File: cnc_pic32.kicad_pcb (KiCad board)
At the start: 4 copper layers, 96 x 96 mm, 133 parts, among them J1 icd, J10 tp_ft232_, J11 tp_ft232_, J12 tp_ft232_, J13 tp_ft232_, J14 tp_ft232_, J15 pololu, J16 pololu, J17 pololu, J18 pololu, J19 pololu, J2 USB_B_Mini, J20 pololu, J21 conector oled ST1306 128x32, J22 Adafruit ST7789, J23 mrf24j40_tp, J24 mrf24j40_tp, J3 tp_ft232_, J4 tp_ft232_, J5 USB_B_Mini, J6 tp_ft232_, J7 tp_ft232_, J8 tp_ft232_, J9 tp_ft232_, Q1 2N7002, SW1 power, SW2 up, SW3 down, SW4 left, SW5 rigth, U1 PIC32MX795F512L-80x-PF, U2 LM1117DT-3.3, U3 FT232BM, U4 LM1117DT-3.3, U5 MRF24J40MA, Y1 8MHZ, Y2 6MHZ

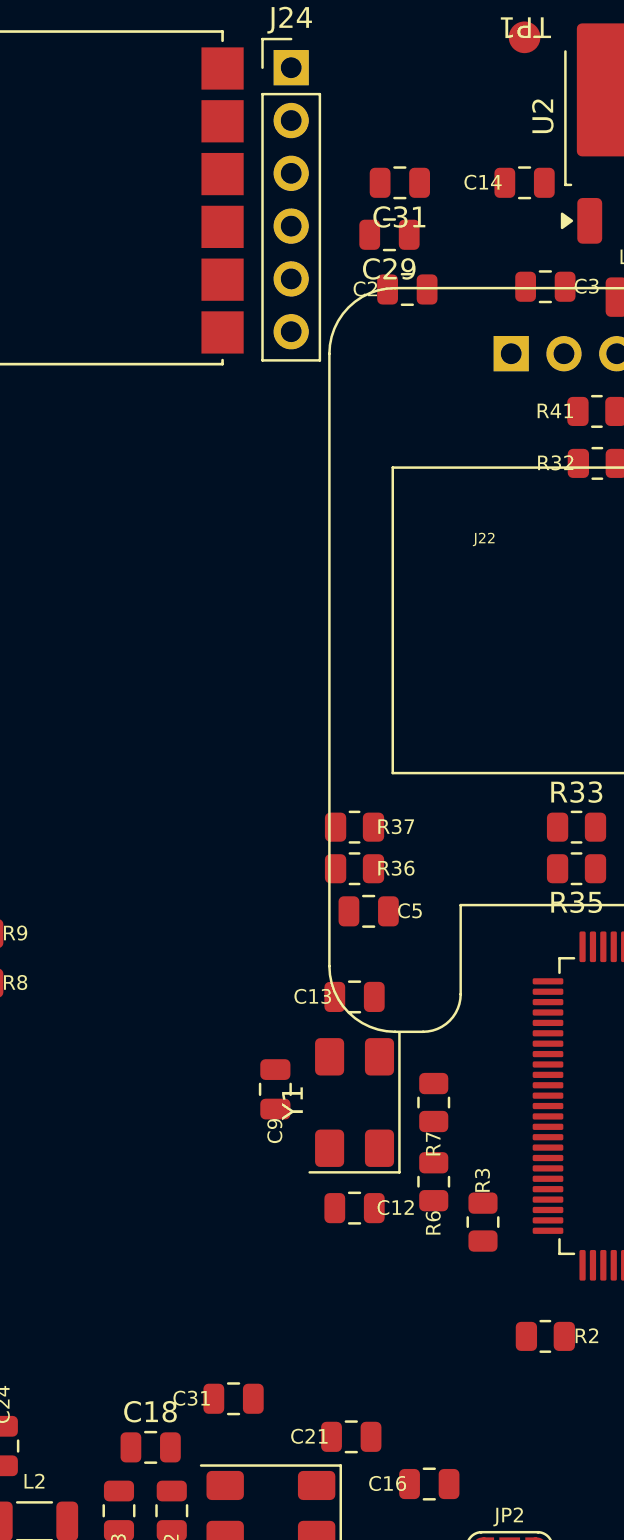
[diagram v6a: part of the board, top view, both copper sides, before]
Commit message: fix: remove duplicate C31 from PCB
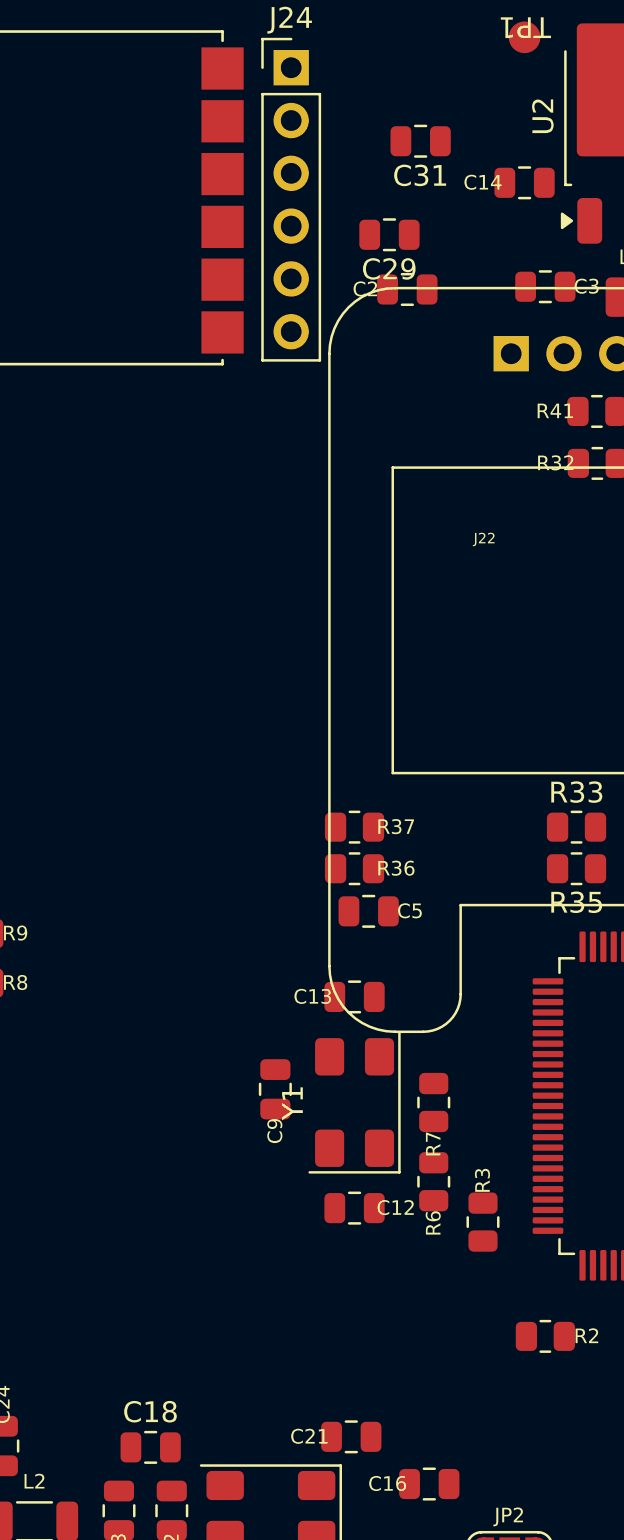
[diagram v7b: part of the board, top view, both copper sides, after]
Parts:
- removed the C31 at (78.0, 93.5)
- moved C31 2.24 mm to (87.0, 33.0)
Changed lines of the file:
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@@
 		)
 	)
-	(footprint "Capacitor_SMD:C_0805_2012Metric"
-		(layer "F.Cu")
-		(at 78 93.5)
-		(descr "Capacitor SMD 0805 (2012 Metric), square (rectangular) end terminal, IPC-7351 nominal, (Body size source: IPC-SM-782 page 76, https://www.pcb-3d.com/wordpress/wp-content/uploads/ipc-sm-782a_amendment_1_and_2.pdf, https://docs.google.com/spreadsheets/d/1BsfQQcO9C6DZCsRaXUlFlo91Tg2WpOkGARC1WS5S8t0/edit?usp=sharing)")
-		(tags "capacitor")
-		(property "Reference" "C31"
-			(at -2 0 0)
-			(layer "F.SilkS")
-			(effects
-				(font
-					(face "Arial")
-					(size 0.7 0.7)
-					(thickness 0.1)
-				)
-			)
-			(render_cache "C31" 0
-				(polygon
-					(pts
-						(xy 75.480764 93.181205) (xy 75.425794 93.186116) (xy 75.379489 93.200024) (xy 75.340185 93.222346)
-						(xy 75.306717 93.253397) (xy 75.280597 93.290873) (xy 75.261246 93.335369) (xy 75.248949 93.388238)
-						(xy 75.244569 93.451167) (xy 75.249039 93.513038) (xy 75.261707 93.566016) (xy 75.281863 93.611569)
-						(xy 75.309367 93.65086) (xy 75.344292 93.683659) (xy 75.384378 93.706983) (xy 75.430649 93.721356)
-						(xy 75.484611 93.726386) (xy 75.530032 93.722431) (xy 75.570486 93.710977) (xy 75.606918 93.692203)
-						(xy 75.640017 93.665715) (xy 75.67016 93.630569) (xy 75.697383 93.585336) (xy 75.772011 93.622778)
-						(xy 75.748537 93.66475) (xy 75.721301 93.70053) (xy 75.690244 93.730749) (xy 75.655111 93.755835)
-						(xy 75.616682 93.775477) (xy 75.575088 93.789691) (xy 75.529833 93.798433) (xy 75.480337 93.801442)
-						(xy 75.41354 93.796428) (xy 75.355269 93.782094) (xy 75.304109 93.759041) (xy 75.269143 93.735556)
-						(xy 75.238809 93.707741) (xy 75.212749 93.67532) (xy 75.190799 93.637823) (xy 75.169704 93.583928)
-						(xy 75.156468 93.522178) (xy 75.151818 93.451167) (xy 75.155749 93.385686) (xy 75.166919 93.328773)
-						(xy 75.184645 93.279202) (xy 75.208603 93.235938) (xy 75.238841 93.198174) (xy 75.275222 93.166025)
-						(xy 75.316658 93.140807) (xy 75.363876 93.122294) (xy 75.417865 93.110691) (xy 75.479824 93.10662)
-						(xy 75.534017 93.109517) (xy 75.581471 93.11776) (xy 75.623074 93.13083) (xy 75.659599 93.148422)
-						(xy 75.693157 93.171689) (xy 75.721836 93.199786) (xy 75.746005 93.233115) (xy 75.765771 93.272332)
-						(xy 75.679217 93.300841) (xy 75.66021 93.264768) (xy 75.635261 93.235404) (xy 75.603905 93.211937)
-						(xy 75.56814 93.19521) (xy 75.527431 93.184832)
-					)
-				)
-				(polygon
-					(pts
-						(xy 76.310823 93.60504) (xy 76.306765 93.651148) (xy 76.295302 93.689809) (xy 76.276963 93.722446)
-						(xy 76.25154 93.750065) (xy 76.220796 93.771418) (xy 76.183303 93.787432) (xy 76.137683 93.797734)
-						(xy 76.082236 93.801442) (xy 76.030765 93.798184) (xy 75.987179 93.789026) (xy 75.950239 93.774637)
-						(xy 75.918917 93.755322) (xy 75.892119 93.73016) (xy 75.871175 93.699656) (xy 75.855865 93.662941)
-						(xy 75.846512 93.61876) (xy 75.935459 93.610639) (xy 75.944756 93.648359) (xy 75.959694 93.677449)
-						(xy 75.979969 93.699647) (xy 76.006147 93.715929) (xy 76.039577 93.726383) (xy 76.082236 93.73019)
-						(xy 76.124477 93.726215) (xy 76.15788 93.715233) (xy 76.184348 93.697962) (xy 76.204299 93.674085)
-						(xy 76.216846 93.64293) (xy 76.221406 93.602219) (xy 76.216536 93.567486) (xy 76.202582 93.53924)
-						(xy 76.179091 93.515879) (xy 76.149237 93.499619) (xy 76.109438 93.488853) (xy 76.05689 93.484848)
-						(xy 76.008121 93.484848) (xy 76.008121 93.410262) (xy 76.054967 93.410262) (xy 76.101253 93.406371)
-						(xy 76.137089 93.39577) (xy 76.164729 93.379445) (xy 76.186239 93.356463) (xy 76.19917 93.328534)
-						(xy 76.203711 93.294088) (xy 76.199894 93.25936) (xy 76.189188 93.231413) (xy 76.17191 93.208731)
-						(xy 76.148778 93.192084) (xy 76.118064 93.181353) (xy 76.077449 93.177401) (xy 76.040549 93.180923)
-						(xy 76.010318 93.190806) (xy 75.985382 93.206594) (xy 75.965587 93.228158) (xy 75.951945 93.255109)
-						(xy 75.94452 93.288788) (xy 75.857967 93.282077) (xy 75.866174 93.2419) (xy 75.880366 93.20759)
-						(xy 75.900383 93.178172) (xy 75.926568 93.152995) (xy 75.957086 93.133289) (xy 75.992011 93.118849)
-						(xy 76.032125 93.109799) (xy 76.07839 93.10662) (xy 76.129448 93.109997) (xy 76.171789 93.119415)
-						(xy 76.206886 93.1341) (xy 76.235938 93.153722) (xy 76.260215 93.179171) (xy 76.277578 93.208898)
-						(xy 76.288351 93.243754) (xy 76.292145 93.284984) (xy 76.287846 93.326641) (xy 76.27569 93.36111)
-						(xy 76.256027 93.389917) (xy 76.229611 93.413082) (xy 76.195228 93.431449) (xy 76.151095 93.44467)
-						(xy 76.151095 93.446593) (xy 76.19968 93.456478) (xy 76.238239 93.473605) (xy 76.268722 93.4975)
-						(xy 76.29197 93.528193) (xy 76.305967 93.563571)
-					)
-				)
-				(polygon
-					(pts
-						(xy 76.428152 93.7905) (xy 76.428152 93.717324) (xy 76.599848 93.717324) (xy 76.599848 93.199798)
-						(xy 76.44777 93.309048) (xy 76.44777 93.227752) (xy 76.607029 93.117562) (xy 76.686402 93.117562)
-						(xy 76.686402 93.717324) (xy 76.850405 93.717324) (xy 76.850405 93.7905)
-					)
-				)
-			)
-		)
-		(property "Value" "33nf"
-			(at 0 0.8 0)
-			(layer "F.Fab")
-			(effects
-				(font
-					(size 0.5 0.5)
-					(thickness 0.15)
-				)
-			)
-		)
-		(property "Datasheet" ""
-			(at 0 0 0)
-			(layer "F.Fab")
-			(hide yes)
-			(effects
-				(font
-					(size 0.5 0.5)
-				)
-			)
-		)
-		(property "Description" ""
-			(at 0 0 0)
-			(layer "F.Fab")
-			(hide yes)
-			(effects
-				(font
-					(size 0.5 0.5)
-				)
-			)
-		)
-		(property ki_fp_filters "C_*")
-		(sheetname "/Ft232/")
-		(sheetfile "ft232.kicad_sch")
-		(units
-			(unit
-				(name "A")
-				(pins "1" "2")
-			)
-		)
-		(attr smd)
-		(duplicate_pad_numbers_are_jumpers no)
-		(fp_line
-			(start -0.261252 -0.735)
-			(end 0.261252 -0.735)
-			(stroke
-				(width 0.12)
-				(type solid)
-			)
-			(layer "F.SilkS")
-		)
-		(fp_line
-			(start -0.261252 0.735)
-			(end 0.261252 0.735)
-			(stroke
-				(width 0.12)
-				(type solid)
-			)
-			(layer "F.SilkS")
-		)
-		(fp_rect
-			(start -1.7 -0.98)
-			(end 1.7 0.98)
-			(stroke
-				(width 0.05)
-				(type solid)
-			)
-			(fill no)
-			(layer "F.CrtYd")
-		)
-		(fp_rect
-			(start -1 -0.625)
-			(end 1 0.625)
-			(stroke
-				(width 0.1)
-				(type solid)
-			)
-			(fill no)
-			(layer "F.Fab")
-		)
-		(fp_text user "${REFERENCE}"
-			(at 0 -0.8 0)
-			(layer "F.Fab")
-			(effects
-				(font
-					(size 0.5 0.5)
-					(thickness 0.08)
-				)
-			)
-		)
-		(pad "1" smd roundrect
-			(at -0.95 0)
-			(size 1 1.45)
-			(layers "F.Cu" "F.Mask" "F.Paste")
-			(roundrect_rratio 0.25)
-			(net "Net-(J3-Pin_1)")
-			(pintype "passive")
-		)
-		(pad "2" smd roundrect
-			(at 0.95 0)
-			(size 1 1.45)
-			(layers "F.Cu" "F.Mask" "F.Paste")
-			(roundrect_rratio 0.25)
-			(net "GND")
-			(pintype "passive")
-		)
-		(embedded_fonts no)
-		(model "${KICAD10_3DMODEL_DIR}/Capacitor_SMD.3dshapes/C_0805_2012Metric.step"
-			(offset
-				(xyz 0 0 0)
-			)
-			(scale
-				(xyz 1 1 1)
-			)
-			(rotate
-				(xyz 0 0 0)
-			)
-		)
-	)
 	(footprint "Jumper:SolderJumper-3_P1.3mm_Open_RoundedPad1.0x1.5mm_NumberLabels"
 		(layer "F.Cu")
@@
 	(footprint "Capacitor_SMD:C_0805_2012Metric"
 		(layer "F.Cu")
-		(at 86 35 180)
+		(at 87 33 180)
 		(descr "Capacitor SMD 0805 (2012 Metric), square (rectangular) end terminal, IPC-7351 nominal, (Body size source: IPC-SM-782 page 76, https://www.pcb-3d.com/wordpress/wp-content/uploads/ipc-sm-782a_amendment_1_and_2.pdf, https://docs.google.com/spreadsheets/d/1BsfQQcO9C6DZCsRaXUlFlo91Tg2WpOkGARC1WS5S8t0/edit?usp=sharing)")
 		(tags "capacitor")

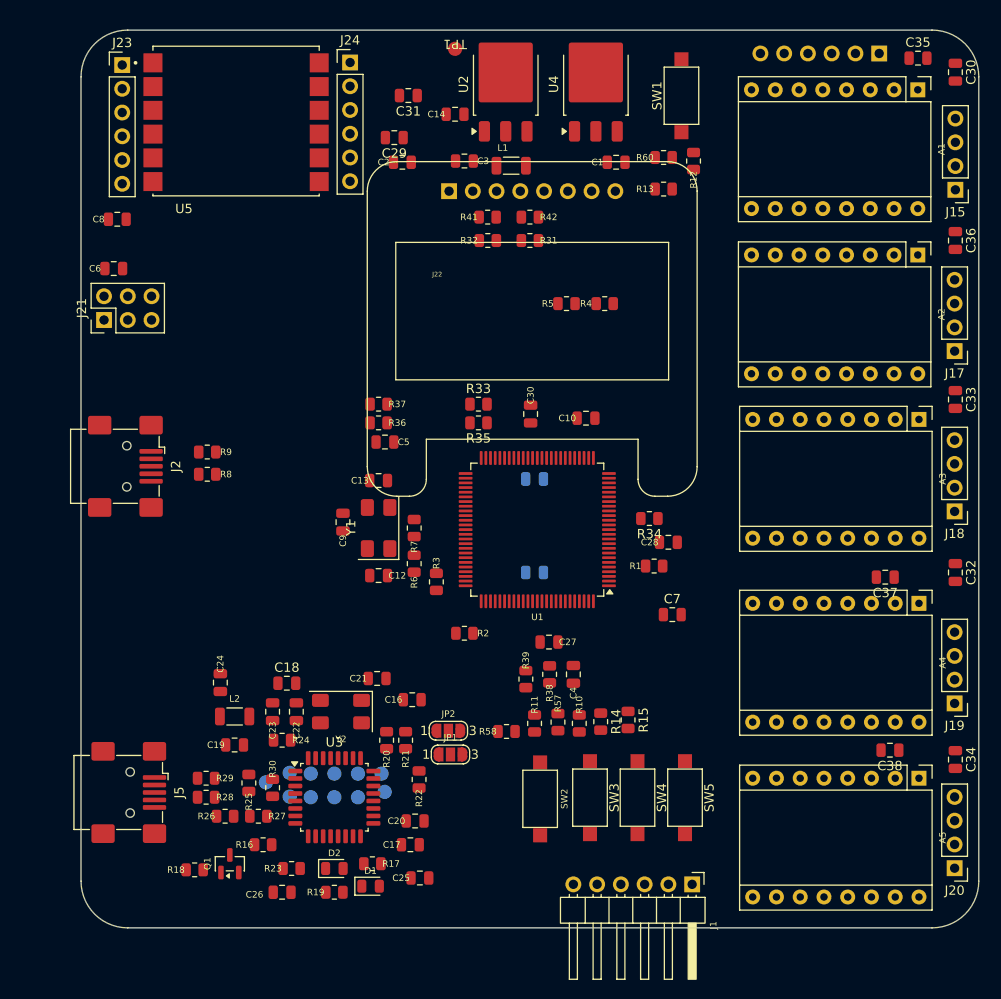
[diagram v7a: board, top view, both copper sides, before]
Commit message: feat: PCB layout updates, schematic changes, remove freerouting.dsn
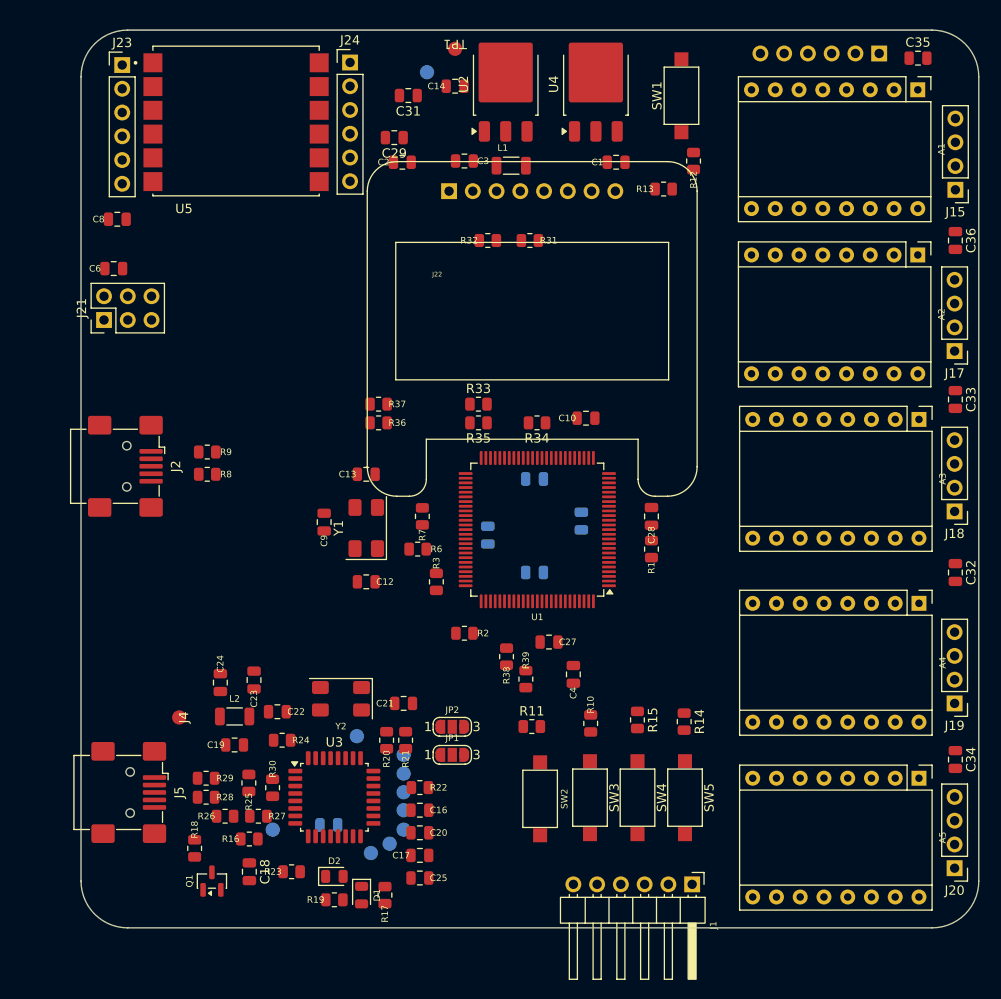
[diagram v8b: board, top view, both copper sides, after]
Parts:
- removed C30 (x2), C37, C38: 100nf, Capacitor_SMD:C_0805_2012Metric
- removed R4: 10K, Resistor_SMD:R_0805_2012Metric
- removed R41, R42: 1k, Resistor_SMD:R_0805_2012Metric
- removed R5: 100, Resistor_SMD:R_0805_2012Metric
- removed R57, R58, R60: 2k2, Resistor_SMD:R_0805_2012Metric
- C26, C5, C7: moved to B.Cu
- J4: moved to F.Cu
- moved J14 76.4 mm to (89.0, 30.5)
- moved C18 20.6 mm to (70.0, 116.0), turned to -90 degrees
- moved R34 15.8 mm to (100.8, 68.0)
- moved C5 14.8 mm to (95.5, 80.0), turned to -90 degrees
- moved C7 14.0 mm to (105.5, 78.5), turned to -90 degrees
- moved J3 12.6 mm to (72.5, 111.5)
- moved J13 12.4 mm to (86.5, 105.5)
- moved C16 11.8 mm to (88.2, 109.4), turned to 180 degrees
- moved J4 11.6 mm to (62.5, 99.5)
- moved J7 10.5 mm to (86.5, 111.5)
- moved R14 8.93 mm to (116.5, 99.9)
- moved C26 8.76 mm to (78.5, 111.0), turned to 180 degrees
- moved J10 8.22 mm to (85.0, 113.0)
- moved J8 7.67 mm to (86.5, 107.5)
- moved J9 7.54 mm to (86.5, 109.4)
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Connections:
- J10 pad 1: /Ft232/tp_ft232/FT_TXD_EN -> /Ft232/FT_TXD_EN
- J11 pad 1: /Ft232/tp_ft232/FT_PWR_EN -> /Ft232/FT_PWR_EN
- J12 pad 1: /Ft232/tp_ft232/FT_RST -> /Ft232/FT_RESET
- J13 pad 1: /Ft232/tp_ft232/FT_DTR -> /Ft232/FT_DTR
- J7 pad 1: /Ft232/tp_ft232/FT_RI -> /Ft232/FT_RI
- J8 pad 1: /Ft232/tp_ft232/FT_DCD -> /Ft232/FT_DCD
- J9 pad 1: /Ft232/tp_ft232/FT_DRS -> /Ft232/FT_DRS
- U3 pad 23: /Ft232/FT_RST -> /Ft232/FT_RESET
